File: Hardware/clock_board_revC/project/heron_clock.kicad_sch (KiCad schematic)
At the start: 110 parts, among them J1 5V_IN, J10 PPS_B200_2, J2 PPS_IN, J3 REF_B210_1, J4 REF_B210_2, J5 REF_B200_1, J6 REF_B200_2, J7 PPS_B210_1, J8 PPS_B210_2, J9 PPS_B200_1, U1 LP5907MFX-3.3/NOPB, U2 TLV75533PDBVR, U3 SiT5155AI-FK-33E0-10.000000, U4 LMK1C1104PWR, U5 SN74LVC1G17DBVR, U6 SN74LVC125APWR

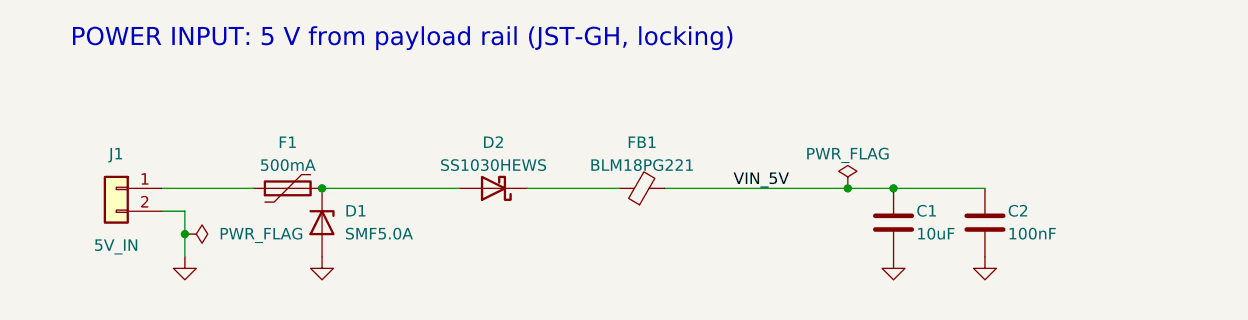
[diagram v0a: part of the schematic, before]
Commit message: Change clock board rev C J1 to JST XH; add CadQuery uv env for the rack
The JST-GH power header SM02B-GHS-TB(LF)(SN) is out of stock at
Digi-Key. J1 is now a JST S2B-XH-A-1(LF)(SN): through-hole, side entry,
friction lock (D-040). The pinout does not change.

- power_conn.py swaps the footprint, places J1 between D2 and J8,
  routes +5 V to the old track, removes 3 GND stitch vias, and moves
  the J1, "+5V IN" and J8 "PPS" silk. make_revc.py calls it.
- New gerbers and fab outputs. DRC: 28 items, no new ones. ERC: 0.
  J1 is not in the CPL file now (through-hole).
- BOM, design.py, README, HARDWARE.md and DECISIONS.md updated.
- Rack models use the XH body. check_fit.py: 0 clashes, mate PASS.
- Hardware/payload_rack is now its own uv project with CadQuery 2.8.
  Run "uv run python check_fit.py" there. CLAUDE.md tells agents how.

Co-Authored-By: Claude Opus 5.5 <noreply@anthropic.com>
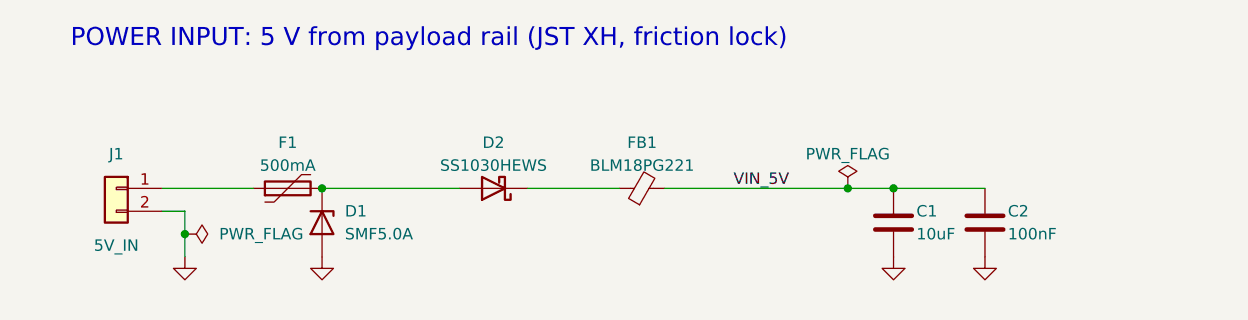
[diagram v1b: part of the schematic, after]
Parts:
- J1: footprint Connector_JST:JST_GH_SM02B-GHS-TB_1x02-1MP_P1.25mm_Horizontal -> Connector_JST:JST_XH_S2B-XH-A-1_1x02_P2.50mm_Horizontal; MPN SM02B-GHS-TB(LF)(SN) -> S2B-XH-A-1(LF)(SN)
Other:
- note added: "POWER INPUT: 5 V from payload rail (JST XH, friction lock)"
- note removed: "POWER INPUT: 5 V from payload rail (JST-GH, locking)"
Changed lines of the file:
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@@
 		(comment 2 "Generated by design.py - edit values there and re-run")
 	)
-	(text "POWER INPUT: 5 V from payload rail (JST-GH, locking)"
+	(text "POWER INPUT: 5 V from payload rail (JST XH, friction lock)"
 		(exclude_from_sim no)
 		(at 20.32 22.86 0)
@@
 			)
 		)
-		(property "Footprint" "Connector_JST:JST_GH_SM02B-GHS-TB_1x02-1MP_P1.25mm_Horizontal"
+		(property "Footprint" "Connector_JST:JST_XH_S2B-XH-A-1_1x02_P2.50mm_Horizontal"
 			(at 25.4 40.64 0)
 			(hide yes)
@@
 			)
 		)
-		(property "MPN" "SM02B-GHS-TB(LF)(SN)"
+		(property "MPN" "S2B-XH-A-1(LF)(SN)"
 			(at 25.4 40.64 0)
 			(hide yes)

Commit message: Add clock board rev D: jacks on the real SDR connectors, USB holes
Photos of a B210 and a B200 show the SDR rear edge order: GPS ANT,
10 MHz, USB-B, PPS, DC jack. The rev C jacks faced GPS ANT and 10 MHz,
so rev C must not be ordered (Q-015 b, D-042).

Rev D (Hardware/clock_board_revD):
- J3-J6 face the SDR 10 MHz SMA, J7-J10 face the PPS SMA.
- Board 118 x 60 mm (rack z 30 to 90). A 16 x 18 mm hole on each
  SDR USB-B axis (a notch at the right edge), with a 2 mm keep-out
  ring so the hole can grow without new layout. DC and GPS ANT stay
  free.
- New generator gen_pcb.py: footprints from the KiCad 10 library,
  hand routes for the filter columns, PPS chains and U3, Freerouting
  1.9.0 for the rest. DRC 0, unconnected 0, footprint errors 0,
  parity 0. ERC 0. No starved thermals, no KiCad 7 footprint notes.
- Same schematic and parts as rev C.

Also in this commit:
- Rev C: D2 gets the Panjit SOD-323HE land (D-041); README marks
  rev C as superseded.
- bom_sources.csv: Digi-Key part numbers from the team order.
- Rack model: 10 MHz/PPS SMA positions corrected, rev D board, USB
  openings in the rear plate. check_fit.py: 0 clashes, all 8 jacks
  0.000 mm. Fusion seed and parts follow.
- DECISIONS.md (D-041, D-042, Q-015), HARDWARE.md, CLAUDE.md.

Co-Authored-By: Claude Opus 5.5 <noreply@anthropic.com>
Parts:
- D2: footprint Diode_SMD:D_SOD-323F -> HERON_Clock:D_SOD-323HE_Panjit
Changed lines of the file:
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@@
 			)
 		)
-		(property "Footprint" "Diode_SMD:D_SOD-323F"
+		(property "Footprint" "HERON_Clock:D_SOD-323HE_Panjit"
 			(at 67.31 40.64 0)
 			(hide yes)
